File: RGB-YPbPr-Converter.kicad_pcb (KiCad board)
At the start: 2 copper layers, 70 x 70 mm, 63 parts, among them J1 Barrel Jack 5.5/2.1, J2 D-Sub HD15 Female, J3 BNC 75 Ohm, J4 BNC 75 Ohm, J5 BNC 75 Ohm, Q1 Q_NPN_BEC, Q2 Q_NPN_BEC, Q3 Q_NPN_BEC, U1 1117-5.0, U2 ICL7660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

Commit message: WIP of sandwich version
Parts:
- removed C4: 100n/16V, Capacitor_SMD:C_0805_2012Metric
- removed R1, R2: 75, Resistor_SMD:R_0805_2012Metric
- removed R18: 0R, Resistor_SMD:R_0805_2012Metric
- added C10: 100n/16V, Capacitor_SMD:C_0603_1608Metric, B.Cu at (142.8, 134.8)
- added C11: 100n/16V, Capacitor_SMD:C_0603_1608Metric, B.Cu at (133.2, 134.7)
- added U5: L7905, Package_TO_SOT_SMD:SOT-89-3, B.Cu at (136.7, 134.8)
- C1, C6, C7: footprint Capacitor_THT:CP_Radial_D5.0mm_P2.00mm -> Capacitor_SMD:C_1206_3216Metric; moved to B.Cu
- C2, C3: footprint Capacitor_SMD:C_0805_2012Metric -> Capacitor_SMD:C_0603_1608Metric; moved to B.Cu
- C5, C8, C9: footprint Capacitor_SMD:C_0805_2012Metric -> Capacitor_SMD:C_0603_1608Metric
- D1: value 1N4001 -> Diode SMA; footprint Diode_THT:D_DO-41_SOD81_P10.16mm_Horizontal -> Diode_SMD:D_SMA
- J1: value Barrel Jack 5.5/2.1 -> ADC-010-1; footprint Connector_BarrelJack:BarrelJack_Horizontal -> lib:ADC-010-1
- J2: footprint lib:ICD15S13E4GV00LF -> Connector_Dsub:DSUB-15-HD_Female_Vertical_P2.29x1.98mm_MountingHoles
- J3, J4, J5: value BNC 75 Ohm -> B01-SPPT4-41BS00; footprint Connector_Coaxial:BNC_Amphenol_B6252HB-NPP3G-50_Horizontal -> lib:B01-SPPT4-41BS00
- Q1, Q2, Q3: value Q_NPN_BEC -> BC847C
- R10: value 549 -> 510R; footprint Resistor_SMD:R_0805_2012Metric -> Resistor_SMD:R_0603_1608Metric
- R11: value 2940 -> 2.7k; footprint Resistor_SMD:R_0805_2012Metric -> Resistor_SMD:R_0603_1608Metric
- R12: value 0R -> 68R; footprint Resistor_SMD:R_0805_2012Metric -> Resistor_SMD:R_0603_1608Metric
- R13: value 0R -> 39R; footprint Resistor_SMD:R_0805_2012Metric -> Resistor_SMD:R_0603_1608Metric
- R14: value 0R -> 240R; footprint Resistor_SMD:R_0805_2012Metric -> Resistor_SMD:R_0603_1608Metric
- R15, R16, R17, R19, R21, R22, R23, R25, R26, R27, R28, R29, R3, R30, R4, R5, R6, R7, R8: footprint Resistor_SMD:R_0805_2012Metric -> Resistor_SMD:R_0603_1608Metric
- R20: value 570 -> 560R; footprint Resistor_SMD:R_0805_2012Metric -> Resistor_SMD:R_0603_1608Metric
- R24: value 1k -> 10k; footprint Resistor_SMD:R_0805_2012Metric -> Resistor_SMD:R_0603_1608Metric
- R9: value 1070 -> 1k; footprint Resistor_SMD:R_0805_2012Metric -> Resistor_SMD:R_0603_1608Metric
- U1: value 1117-5.0 -> L7805; footprint Package_TO_SOT_SMD:SOT-223 -> Package_TO_SOT_SMD:SOT-89-3; moved to B.Cu
- U2: moved to B.Cu
- moved kibuzzard-63377B96 85.9 mm to (54.5, 77.9)
- moved R22 80.0 mm to (67.4, 110.8), turned to 90 degrees
- moved R27 74.0 mm to (75.6, 109.8), turned to -90 degrees
- moved R25 72.5 mm to (77.6, 109.8), turned to 90 degrees
- moved R28 69.9 mm to (75.6, 113.3), turned to -90 degrees
- moved R26 68.7 mm to (83.0, 109.8), turned to 90 degrees
- moved R21 68.3 mm to (77.6, 113.3), turned to 90 degrees
- moved R29 67.5 mm to (85.0, 109.8), turned to -90 degrees
- moved R23 64.3 mm to (83.0, 113.3), turned to 90 degrees
- moved R30 63.0 mm to (85.0, 113.3), turned to -90 degrees
- moved C8 62.0 mm to (76.4, 119.8), turned to -90 degrees
- moved kibuzzard-633F4DF1 61.1 mm to (158.6, 130.3)
- moved R20 60.5 mm to (89.5, 113.3), turned to 180 degrees
- moved U4 59.2 mm to (79.6, 119.8), turned to 90 degrees
- moved C9 56.6 mm to (82.8, 119.8), turned to -90 degrees
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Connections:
- net /B renamed /Conversion Board/B
- net /CAP+ renamed /Input Board/CAP+
- net /CAP- renamed /Input Board/CAP-
- net /FB renamed /Conversion Board/FB
- net /G renamed /Conversion Board/G
- net /H_R renamed /Input Board/H_R
- net /H_SYNC renamed /Input Board/H_SYNC
- net /Pb renamed /Conversion Board/Pb
- net /Pb_OUT renamed /Conversion Board/Pb_OUT
- net /Pr renamed /Conversion Board/Pr
- net /Pr_OUT renamed /Conversion Board/Pr_OUT
- net /R renamed /Conversion Board/R
- net /VIN renamed /Input Board/VIN
- net /V_R renamed /Input Board/V_R
- net /V_SYNC renamed /Input Board/V_SYNC
- net /Y renamed /Conversion Board/Y
- net /YAMP renamed /Conversion Board/YAMP
- net /YSUM renamed /Conversion Board/YSUM
- net /Y_OUT renamed /Conversion Board/Y_OUT
- net Net-(Q3-Pad3) renamed /Conversion Board/SYNC
- C1 pad 1: /VIND -> +12V
- C2 pad 1: /VIND -> +12V
- C5 pad 1: /+5VAMP -> +5V
- C7 pad 2: -5V -> -12V
- D1 pad 1: /VIND -> +12V
- R24 pad 2: +5V -> +12V
- U1 pad 1: GND -> +12V
- U1 pad 2: +5V -> GND
- U1 pad 3: /VIND -> +5V
- U2 pad 5: -5V -> -12V
- U2 pad 8: +5V -> +12V
- U3 pad 5: /+5VAMP -> +5V
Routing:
- net +5V: track 216.1 -> 0.00 mm
- net -5V: track 55.4 -> 0.00 mm
- net GND: track 54.4 -> 0.00 mm, vias 16 -> 0
- net /Input Board/V_SYNC: track 45.3 -> 0.00 mm
- net /Input Board/H_SYNC: track 34.9 -> 0.00 mm
- net /Conversion Board/R: track 33.9 -> 0.00 mm
- net /Conversion Board/B: track 33.1 -> 0.00 mm
- net /Conversion Board/Y: track 32.1 -> 0.00 mm
- net /Conversion Board/Pr: track 28.9 -> 0.00 mm
- net /Conversion Board/Y_OUT: track 22.2 -> 0.00 mm
- net /VIND: track 19.7 -> 0.00 mm
- net /Conversion Board/Pb: track 17.1 -> 0.00 mm
- net /Conversion Board/YSUM: track 16.3 -> 0.00 mm
- net Net-(D2-Pad1): track 14.3 -> 0.00 mm
- net /Conversion Board/G: track 9.47 -> 0.00 mm
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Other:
- board size 70 x 70 mm -> 52 x 70 mm

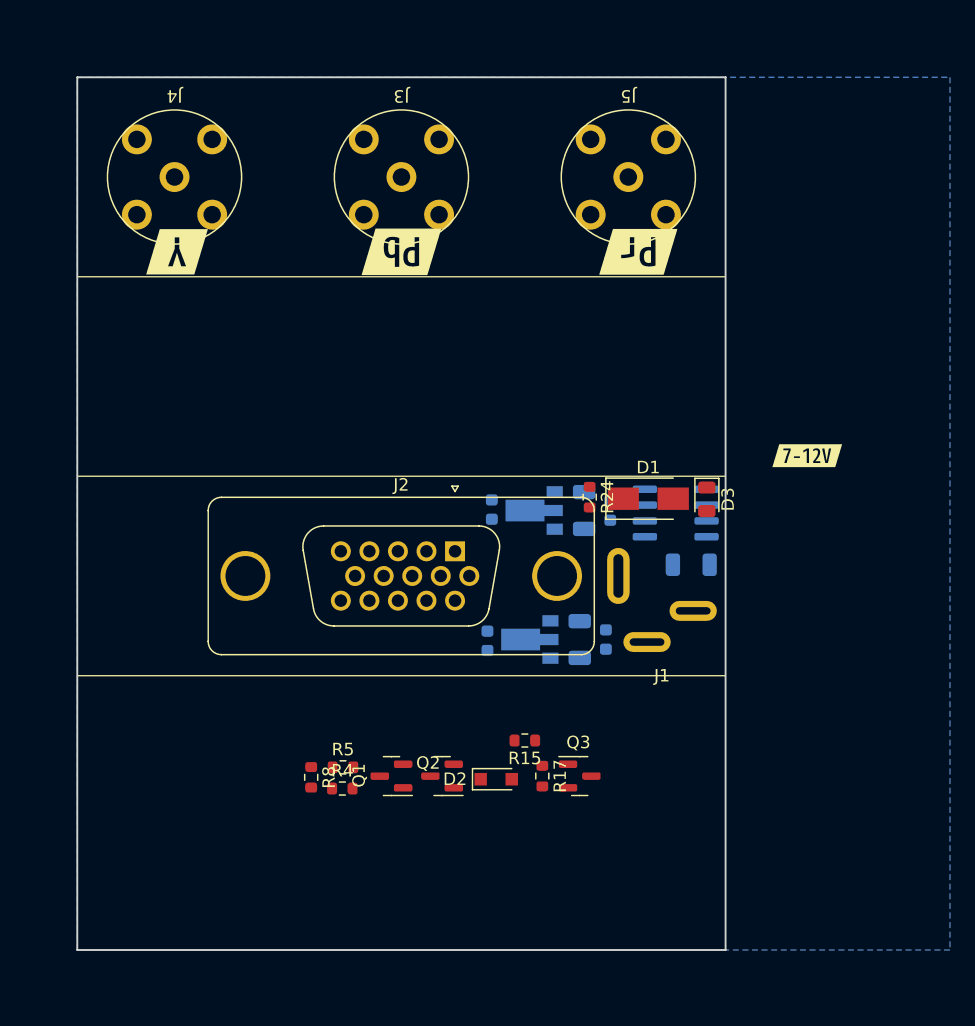
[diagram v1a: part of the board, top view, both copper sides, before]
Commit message: add more 3D models
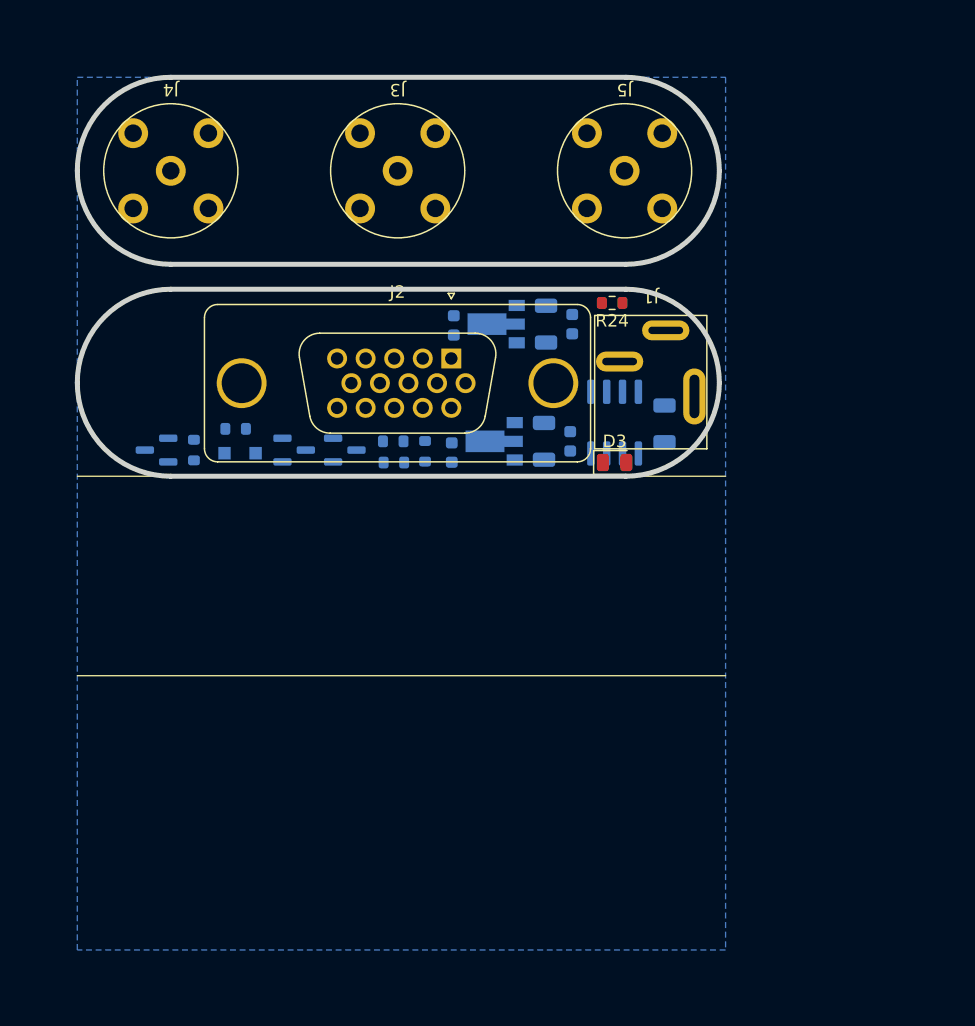
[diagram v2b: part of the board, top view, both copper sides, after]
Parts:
- removed D1: Diode SMA, Diode_SMD:D_SMA
- removed kibuzzard-633F44A8: G***, kibuzzard-633F44A8
- removed kibuzzard-633F44BA: G***, kibuzzard-633F44BA
- removed kibuzzard-633F44C9: G***, kibuzzard-633F44C9
- added kibuzzard-6396650B: G***, kibuzzard-6396650B, B.Cu at (107.5, 113.5)
- added kibuzzard-63966514: G***, kibuzzard-63966514, B.Cu at (125.5, 113.5)
- added kibuzzard-6396651D: G***, kibuzzard-6396651D, B.Cu at (144.0, 113.5)
- D2, Q1, Q2, Q3, R15, R17, R4, R5, R8, kibuzzard-633F4DF1: moved to B.Cu
- moved Q3 42.8 mm to (106.4, 129.9), turned to 180 degrees
- moved R17 38.3 mm to (109.4, 129.9)
- moved R15 34.1 mm to (112.7, 128.2)
- moved D2 33.3 mm to (113.1, 130.2), turned to 180 degrees
- moved Q2 28.7 mm to (117.4, 129.9), turned to 0 degrees
- moved R8 27.7 mm to (127.9, 130.0)
- moved R4 26.5 mm to (125.4, 130.9), turned to 180 degrees
- moved R5 26.5 mm to (125.3, 129.2), turned to 180 degrees
- moved Q1 26.4 mm to (121.5, 129.9), turned to 0 degrees
- moved C1 25.4 mm to (137.6, 119.8)
- moved C2 25.4 mm to (139.7, 119.8)
- moved U1 25.4 mm to (133.6, 119.8)
- moved C3 25.4 mm to (130.2, 119.9)
- moved R24 15.7 mm to (142.9, 118.1), turned to 180 degrees
- moved J2 15.5 mm to (130.0, 122.6)
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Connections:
- J1 pad 1: /Input Board/VIN -> +12V
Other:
- board size 52 x 70 mm -> 51.5 x 32 mm

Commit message: WIP
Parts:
- removed H1, H2, H3, H4: DNP, MountingHole:MountingHole_3.2mm_M3_ISO7380_Pad
- added J6: Conn_01x05_Male, Connector_PinHeader_2.54mm:PinHeader_1x05_P2.54mm_Vertical, F.Cu at (116.5, 112.4)
- added J7: Conn_01x05_Female, Connector_PinSocket_2.54mm:PinSocket_1x05_P2.54mm_Vertical, F.Cu at (116.5, 119.8)
- added J8: Conn_01x03_Male, Connector_PinHeader_2.54mm:PinHeader_1x03_P2.54mm_Vertical, F.Cu at (134.7, 109.9)
- added J9: Conn_01x03_Female, Connector_PinSocket_2.54mm:PinSocket_1x03_P2.54mm_Vertical, F.Cu at (134.6, 122.2)
- C1, C10, C11, C2, C3, C6, C7, D2, Q1, Q2, Q3, R15, R17, R4, R5, R8, U1, U2, U5, kibuzzard-633F4DF1, kibuzzard-6396650B, kibuzzard-63966514, kibuzzard-6396651D: moved to F.Cu
- D3, J1, J2, J3, J4, J5, R24: moved to B.Cu
- moved D3 29.8 mm to (143.1, 101.1)
- moved R4 29.8 mm to (125.4, 101.1)
- moved D2 28.3 mm to (113.1, 101.8)
- moved C11 28.2 mm to (130.0, 101.9), turned to -90 degrees
- moved R8 28.0 mm to (127.9, 102.0), turned to 90 degrees
- moved Q1 27.8 mm to (121.5, 102.1)
- moved Q2 27.8 mm to (117.4, 102.1)
- moved Q3 27.8 mm to (106.4, 102.1)
- moved R17 27.8 mm to (109.4, 102.1), turned to 90 degrees
- moved C10 26.4 mm to (139.5, 102.8), turned to -90 degrees
- moved C7 26.4 mm to (137.4, 102.8), turned to 90 degrees
- moved R5 26.4 mm to (125.3, 102.8)
- moved U5 26.4 mm to (133.4, 102.8)
- moved R15 24.4 mm to (112.7, 103.8)
- moved C6 23.6 mm to (147.1, 104.2), turned to -90 degrees
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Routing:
- added copper zone on F.Cu, net GND
- removed copper zone on B.Cu, net GND

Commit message: WIP
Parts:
- added J10: 690357101072, lib:690357101072, F.Cu at (116.6, 127.5)
- added J11: 690367181072, lib:690367181072, B.Cu at (116.6, 107.5)
- added J12: 690357101072, lib:690357101072, B.Cu at (140.1, 87.3)
- added J13: 690367181072, lib:690367181072, F.Cu at (177.5, 104.7)
- added J14: L77HDEH15SOL2RM8C309, lib:AMPHENOL_L77HDEH15SOL2RM8C309, F.Cu at (125.5, 107.4)
- J1, J2: moved to F.Cu
- J6: value Conn_01x05_Male -> 690357101072; footprint Connector_PinHeader_2.54mm:PinHeader_1x05_P2.54mm_Vertical -> lib:690357101072
- J7: value Conn_01x05_Female -> 690367181072; footprint Connector_PinSocket_2.54mm:PinSocket_1x05_P2.54mm_Vertical -> lib:690367181072; moved to B.Cu
- J8: value Conn_01x03_Male -> 690357101072; footprint Connector_PinHeader_2.54mm:PinHeader_1x03_P2.54mm_Vertical -> lib:690357101072; moved to B.Cu
- J9: value Conn_01x03_Female -> 690367181072; footprint Connector_PinSocket_2.54mm:PinSocket_1x03_P2.54mm_Vertical -> lib:690367181072
- moved C1 78.7 mm to (74.1, 65.6)
- moved C10 78.7 mm to (76.1, 56.2)
- moved C11 78.7 mm to (66.6, 55.3)
- moved C2 78.7 mm to (76.2, 65.6)
- moved C3 78.7 mm to (66.7, 65.5)
- moved C6 78.7 mm to (83.6, 57.6)
- moved C7 78.7 mm to (74.0, 56.2)
- moved D2 78.7 mm to (49.6, 55.3)
- moved Q1 78.7 mm to (58.0, 55.5)
- moved Q2 78.7 mm to (53.9, 55.5)
- moved R15 78.7 mm to (49.2, 57.2)
- moved R24 78.7 mm to (79.4, 67.3)
- moved R4 78.7 mm to (61.9, 54.5)
- moved R8 78.7 mm to (64.4, 55.4)
- moved U1 78.7 mm to (70.1, 65.6)
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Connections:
- J6 pad 1: /Conversion Board/R -> unconnected-(J6-Pad1)
- J6 pad 2: /Conversion Board/G -> unconnected-(J6-Pad2)
- J6 pad 3: GND -> unconnected-(J6-Pad3)
- J6 pad 4: /Conversion Board/B -> unconnected-(J6-Pad4)
- J6 pad 5: /Conversion Board/SYNC -> unconnected-(J6-Pad5)
- J7 pad 1: /Conversion Board/R -> unconnected-(J7-Pad1)
- J7 pad 2: /Conversion Board/G -> unconnected-(J7-Pad2)
- J7 pad 3: GND -> unconnected-(J7-Pad3)
- J7 pad 4: /Conversion Board/B -> unconnected-(J7-Pad4)
- J7 pad 5: /Conversion Board/SYNC -> unconnected-(J7-Pad5)
- J8 pad 1: +5V -> unconnected-(J8-Pad1)
- J8 pad 2: GND -> unconnected-(J8-Pad2)
- J8 pad 3: -5V -> unconnected-(J8-Pad3)
- J9 pad 1: +5V -> unconnected-(J9-Pad1)
- J9 pad 2: GND -> unconnected-(J9-Pad2)
- J9 pad 3: -5V -> unconnected-(J9-Pad3)
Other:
- board size 51.5 x 32 mm -> 51.5 x 55 mm
- board text added: "blackwine/Miły/Kosmolot Decrunch 2023"
- board text removed: "blackwine/Miły/Kosmolot Decrunch 2022"
